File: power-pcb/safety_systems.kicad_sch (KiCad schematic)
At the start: 41 parts, among them J12 Conn_01x06, J13 Conn_01x03, J15 Conn_01x02, J17 Screw_Terminal_01x04, J18 Screw_Terminal_01x02, K1 G5Q-1A, K2 G5Q-1A, Q1 AO3400A, Q2 AO3400A, Q3 AO3400A, U22 NCV7357D13R2G, U23 74AHC1G08

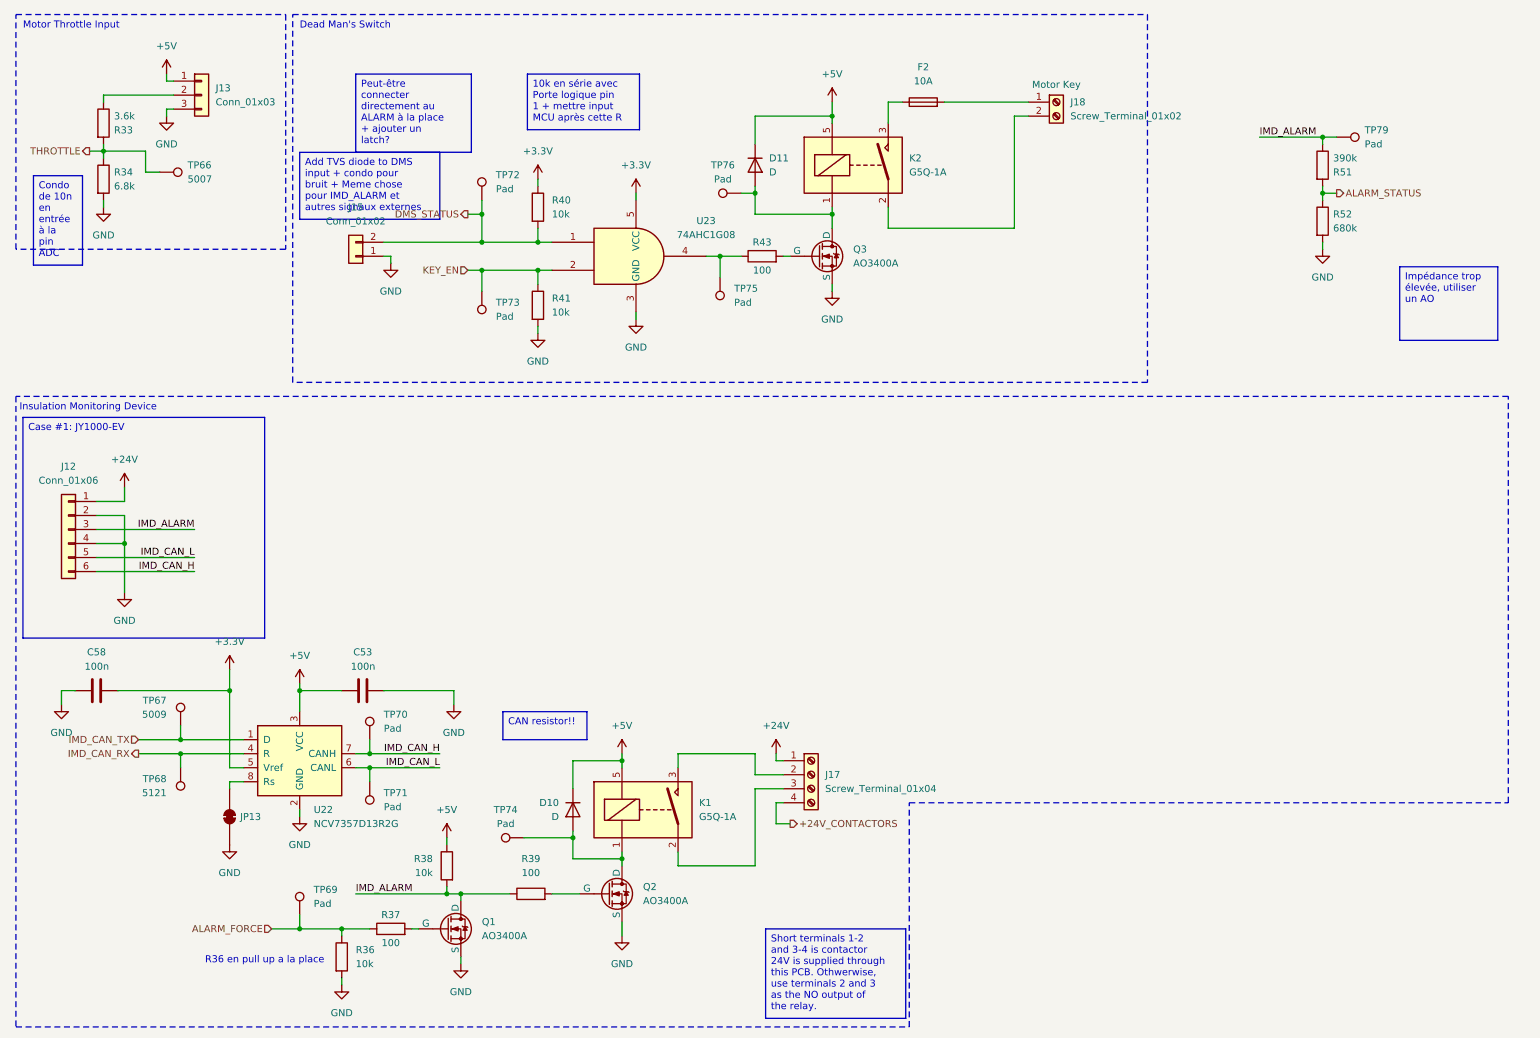
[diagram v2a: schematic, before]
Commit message: power-pcb: finish schematic layout
All parts are placed and connected, ERC passes (except for two
exclusions with comment).
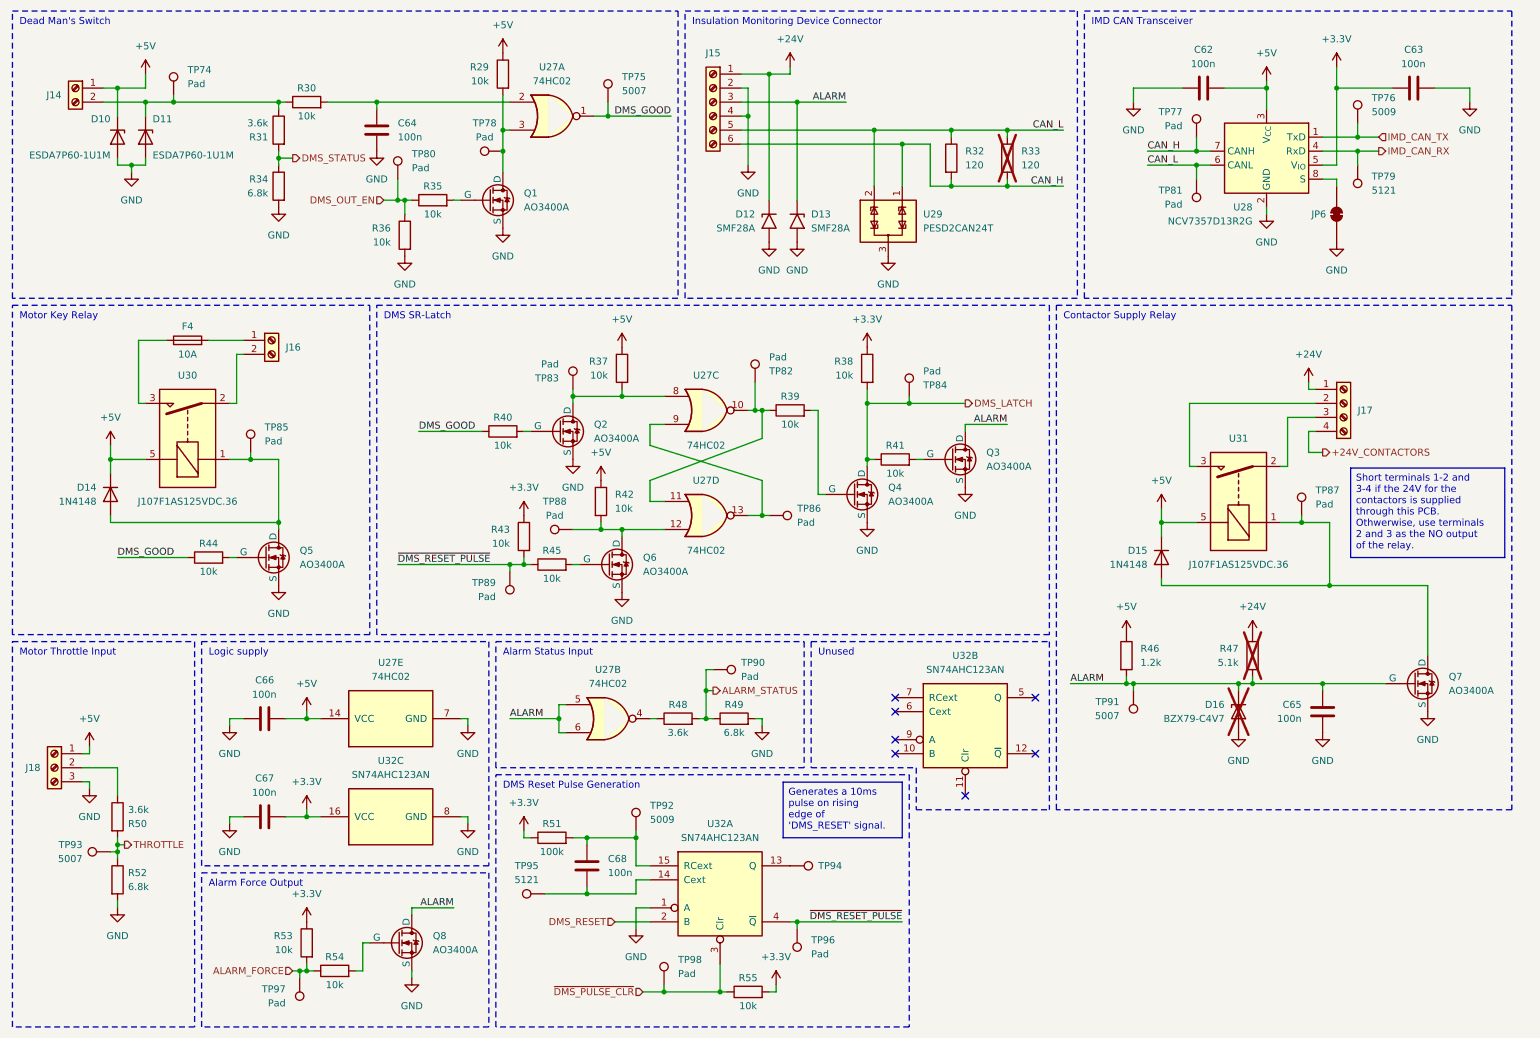
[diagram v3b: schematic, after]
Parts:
- removed C53, C58: 100n, Capacitor_SMD:C_0603_1608Metric_Pad1.08x0.95mm_HandSolder, symbol Device:C
- removed D10: D, symbol Device:D
- removed J12: Conn_01x06, symbol Connector_Generic:Conn_01x06
- removed J13: Conn_01x03, symbol Connector_Generic:Conn_01x03
- removed J15: Conn_01x02, symbol Connector_Generic:Conn_01x02
- removed JP13: SolderJumper_2_Bridged, symbol Jumper:SolderJumper_2_Bridged
- removed K1, K2: G5Q-1A, Relay_THT:Relay_SPST_Omron-G5Q-1A, symbol Relay:G5Q-1A
- removed R52: 680k, Resistor_SMD:R_0603_1608Metric, symbol Device:R
- removed TP67: 5009, symbol Connector:TestPoint
- removed TP68: 5121, symbol Connector:TestPoint
- removed TP70, TP71, TP72, TP73: Pad, symbol Connector:TestPoint
- removed U22: NCV7357D13R2G, Package_SO:SOIC-8_3.9x4.9mm_P1.27mm, symbol Interface_CAN_LIN:SN65HVD230
- removed U23: 74AHC1G08, symbol 74xGxx:74AHC1G08
- added C62, C63, C64, C65, C66, C67: 100n, Capacitor_SMD:C_0603_1608Metric_Pad1.08x0.95mm_HandSolder, symbol Device:C
- added C68: 100n, symbol Device:C
- added D10, D11: ESDA7P60-1U1M, symbol Device:D_Zener
- added D12, D13: SMF28A, Diode_SMD:D_SMF, symbol Diode:SMF28A
- added D15: 1N4148, Diode_THT:D_DO-35_SOD27_P7.62mm_Horizontal, symbol Device:D
- added D16: BZX79-C4V7, symbol Device:D_Zener
- added J14: Screw_Terminal_01x02, symbol Connector:Screw_Terminal_01x02
- added J15: Screw_Terminal_01x06, symbol Connector:Screw_Terminal_01x06
- added J18: Screw_Terminal_01x03, symbol Connector:Screw_Terminal_01x03
- added JP6: SolderJumper_2_Bridged, symbol Jumper:SolderJumper_2_Bridged
- added Q1, Q3, Q4, Q6, Q7: AO3400A, Package_TO_SOT_SMD:SOT-23, symbol Simulation_SPICE:NMOS
- added R29, R30, R35, R36, R42, R44, R45, R54, R55: 10k, symbol Device:R
- added R31, R48: 3.6k, Resistor_SMD:R_0603_1608Metric, symbol Device:R
- added R32, R33: 120, symbol Device:R
- added R34, R49: 6.8k, Resistor_SMD:R_0603_1608Metric, symbol Device:R
- added R46: 1.2k, Resistor_SMD:R_0402_1005Metric, symbol Device:R
- added R47: 5.1k, symbol Device:R
- added TP76, TP92: 5009, symbol Connector:TestPoint
- added TP77, TP78, TP80, TP81, TP82, TP83, TP84, TP86, TP87, TP88, TP89, TP90, TP96, TP98: Pad, symbol Connector:TestPoint
- added TP91: 5007, symbol Connector:TestPoint
- added TP94: TestPoint, TestPoint:TestPoint_THTPad_D2.0mm_Drill1.0mm, symbol Connector:TestPoint
- added TP95: 5121, symbol Connector:TestPoint
- added U27: 74HC02, symbol 74xx:74HC02
- added U28: NCV7357D13R2G, Package_SO:SOIC-8_3.9x4.9mm_P1.27mm, symbol Exocet:NCV7357
- added U29: PESD2CAN24T, Package_TO_SOT_SMD:SOT-23_Handsoldering, symbol Exocet:PESD2CAN
- added U30, U31: J107F1AS125VDC.36, Relay_THT:Relay_SPDT_Omron-G5LE-1, symbol Exocet:J107F1AS
- added U32: SN74AHC123AN, Package_DIP:DIP-16_W7.62mm_LongPads, symbol 74xx:74AHCT123
- D14: renamed from D11; value D -> 1N4148; footprint (none) -> Diode_THT:D_DO-35_SOD27_P7.62mm_Horizontal
- R37, R39, R43: value 100 -> 10k
- R51: value 390k -> 100k; footprint Resistor_SMD:R_0603_1608Metric -> (none)
- TP75: value Pad -> 5007
- TP79: value Pad -> 5121
- renumbered F2 to F4, J18 to J16, Q3 to Q5, Q1 to Q8, R33 to R50, R34 to R52, R36 to R53, TP76 to TP85, TP66 to TP93, TP69 to TP97
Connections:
- net +24V: now also D12.1 (A1), J15.1 (Pin_1), R47.1
- net +3.3V: now also R38.1, R43.1, R51.1, R53.1, C63.1, C67.2, R55.2, U28.5 (V_{IO}), U32.16 (VCC); no longer R40.1
- net +5V: now also R37.1, C62.2, C66.2, D10.1 (K), D15.1 (K), J14.1 (Pin_1), J18.1 (Pin_1), R29.1, R42.1, R46.1, U27.14 (VCC), U28.3 (V_{CC}), U30.5, U31.5; no longer R38.1
- net ALARM_FORCE: now also R53.2, R54.1; no longer R37.1, R53.1
- net ALARM_STATUS: now also R48.2, R49.1, TP90.1; no longer R51.2
- net DMS_STATUS: now also R31.2, R34.1; no longer R40.2
- net GND: now also C62.1, C63.2, C64.2, C65.2, C66.1, C67.1, D10.2 (A), D11.2 (A), D12.2 (A2), D13.2 (A2), D16.2 (A), J15.2 (Pin_2), J15.4 (Pin_4), J18.3 (Pin_3), JP6.1 (A), Q1.3 (S), Q3.3 (S), Q4.3 (S), Q6.3 (S), Q7.3 (S), R34.2, R36.2, R49.2, U27.7 (GND), U28.2 (GND), U29.3, U32.1 (A), U32.8 (GND); no longer R41.2, R53.2
- net IMD_CAN_RX: now also TP79.1, U28.4 (RxD)
- net IMD_CAN_TX: now also TP76.1, U28.1 (TxD)
- net at J17.2 (Pin_2): now also U31.3
- net at J17.3 (Pin_3): now also U31.2
- net at R37.2: now also Q2.1 (D), TP83.1, U27.8; no longer Q8.2 (G)
- net at D14.2 (A), Q5.1 (D), TP85.1: now also U30.1
- net at J16.2 (Pin_2): now also U30.2
- net at F4.1: now also U30.3
- net at TP74.1: now also D11.1 (K), J14.2 (Pin_2), R30.1, R31.1; no longer Q2.1 (D)
- net DMS_GOOD: now reaches TP75.1
- net DMS_GOOD: now also R40.1, R44.1, U27.1; no longer R43.1
- net at Q5.2 (G): now also R44.2; no longer R43.2
- net at Q2.2 (G): now also R40.2; no longer R39.2
- net at R50.1: now also J18.2 (Pin_2)
- removed net IMD_ALARM: Q8.1 (D), R38.2, R39.1, R51.1, TP79.1
- net KEY_EN renamed DMS_LATCH
- net DMS_LATCH: now also R38.2, Q4.1 (D), TP84.1
- new net: R48.1, U27.4
- new net: TP86.1, U27.13, U27.9
- new net: JP6.2 (B), U28.8 (S)
- new net: Q1.2 (G), R35.2
- new net: Q6.1 (D), R42.2, TP88.1, U27.12
- new net: C68.2, TP95.1, U32.14 (Cext)
- new net: D15.2 (A), Q7.1 (D), TP87.1, U31.1
- new net: R39.1, TP82.1, U27.10, U27.11
- new net: Q4.2 (G), R39.2
- new net: C68.1, R51.2, TP92.1, U32.15 (RCext)
- new net: Q8.2 (G), R54.2
- new net: Q6.2 (G), R45.2
- new net: TP94.1, U32.13 (Q)
- new net: Q3.2 (G), R41.2
- new net: Q1.1 (D), R29.2, TP78.1, U27.3
- new net: C64.1, R30.2, U27.2
- new net ALARM: C65.1, D13.1 (A1), D16.1 (K), J15.3 (Pin_3), Q3.1 (D), Q7.2 (G), Q8.1 (D), R46.2, R47.2, TP91.1, U27.5, U27.6
- new net CAN_H: J15.6 (Pin_6), R32.2, R33.2, TP77.1, U28.7 (CANH), U29.1
- new net CAN_L: J15.5 (Pin_5), R32.1, R33.1, TP81.1, U28.6 (CANL), U29.2
- new net DMS_OUT_EN: R35.1, R36.1, TP80.1
- new net DMS_RESET: U32.2 (B)
- new net ~{DMS_PULSE_CLR}: R55.1, TP98.1, U32.3 (Clr)
- new net ~{DMS_RESET_PULSE}: R43.2, R45.1, TP89.1, TP96.1, U32.4 (~{Q})
- no-connect marks 0 -> 7
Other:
- note added: "Alarm Force Output"
- note added: "Alarm Status Input"
- note added: "Contactor Supply Relay"
- note added: "DMS Reset Pulse Generation"
- note added: "DMS SR-Latch"
- note added: "IMD CAN Transceiver"
- note added: "Insulation Monitoring Device Connector"
- note added: "Logic supply"
- note added: "Motor Key Relay"
- note added: "Unused"
- note removed: "Insulation Monitoring Device"
- note removed: "R36 en pull up a la place"
- moved on the sheet: D14, F4, J16, J17, Q5, Q8, R50, R52, R53, TP85, TP93, TP97

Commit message: power-pcb: finish assigning JLCPCB PN
Also assigned missing footprints.
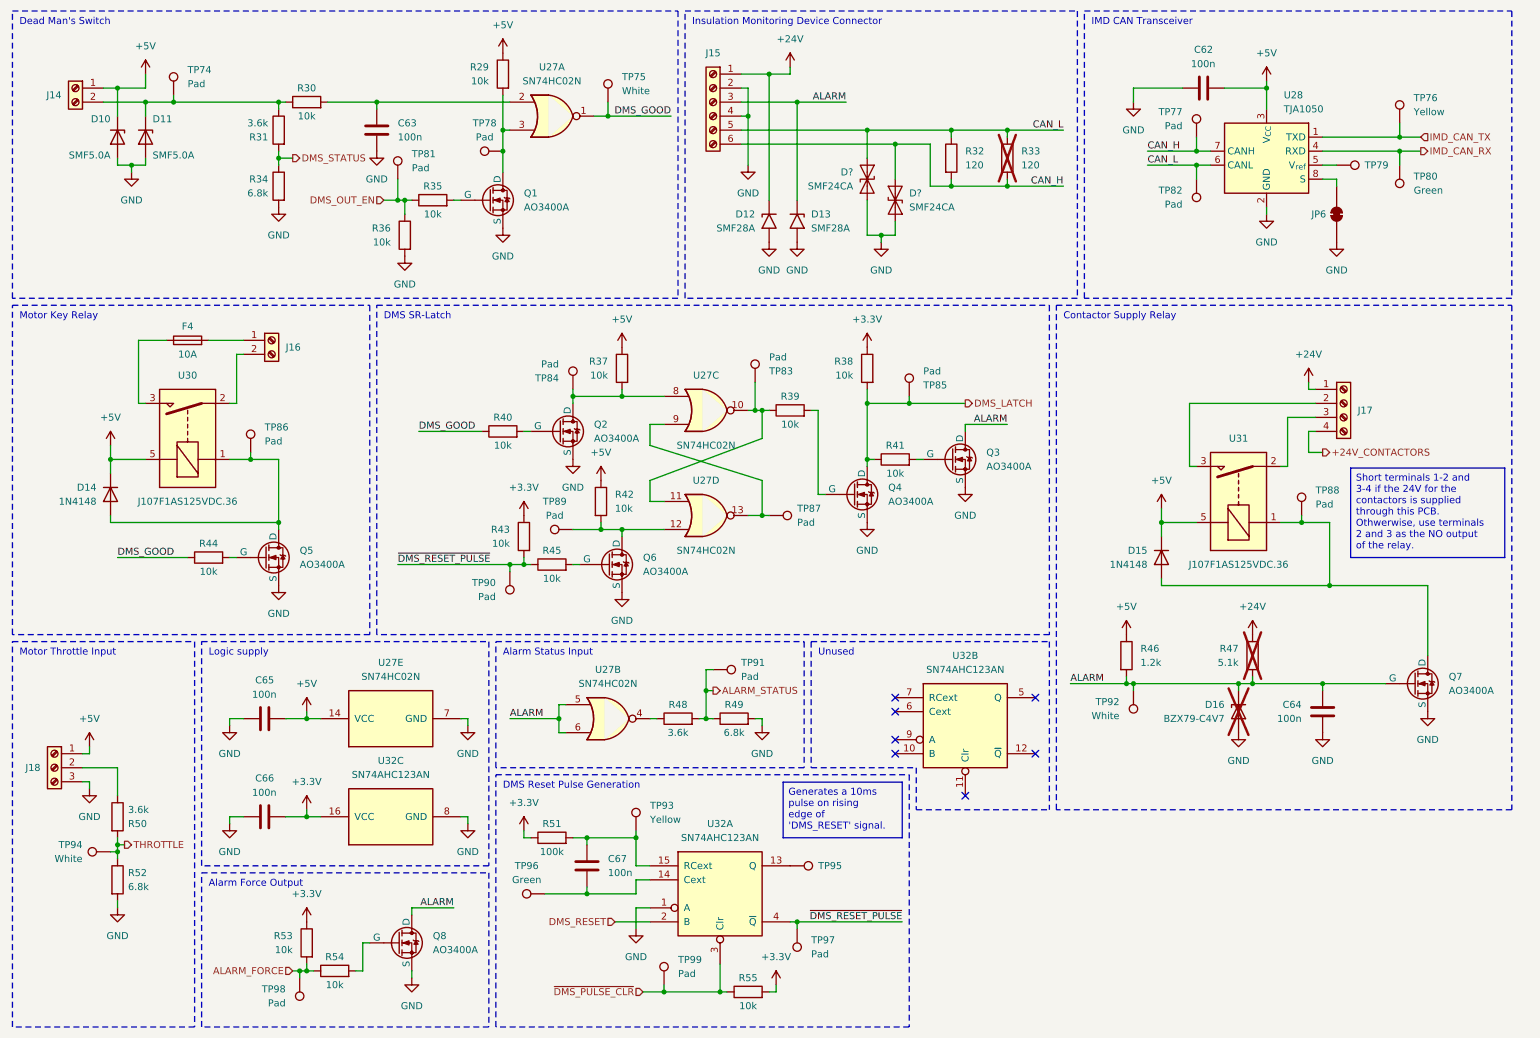
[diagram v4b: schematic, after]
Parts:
- removed C63: 100n, Capacitor_SMD:C_0603_1608Metric_Pad1.08x0.95mm_HandSolder, symbol Device:C
- removed U28: NCV7357D13R2G, Package_SO:SOIC-8_3.9x4.9mm_P1.27mm, symbol Exocet:NCV7357
- removed U29: PESD2CAN24T, Package_TO_SOT_SMD:SOT-23_Handsoldering, symbol Exocet:PESD2CAN
- added D? (x2): SMF24CA, Diode_SMD:D_SOD-123F, symbol Diode:SMAJ24CA
- added TP79: Hole, TestPoint:TestPoint_THTPad_D2.0mm_Drill1.0mm, symbol Connector:TestPoint
- added U28: TJA1050, Package_SO:SOIC-8_3.9x4.9mm_P1.27mm, symbol Exocet:TJA1050
- C67: renamed from C68; footprint (none) -> Capacitor_SMD:C_0603_1608Metric_Pad1.08x0.95mm_HandSolder; JLCPCB (none) -> C14663
- D10, D11: value ESDA7P60-1U1M -> SMF5.0A; footprint (none) -> Diode_SMD:D_SOD-123F; JLCPCB C1975146 -> C19077497
- D12, D13: JLCPCB (none) -> C41376091
- D14, D15: MFR (none) -> onsemi; MPN (none) -> 1N4148
- D16: footprint (none) -> Diode_THT:D_DO-35_SOD27_P7.62mm_Horizontal; MFR (none) -> Nexperia USA Inc.; MPN (none) -> BZX79-C4V7,133
- F4: footprint (none) -> Exocet:Fuseholder_Littelfuse_Combined; MFR (none) -> Littelfuse Inc.; MPN (none) -> 01110501Z
- J14, J16: footprint (none) -> Exocet:Wuerth_Term_Blk_2pos_Side_Entry_5mm; MFR (none) -> Wuerth Eletronik; MPN (none) -> 691137710002
- J15: footprint (none) -> Exocet:Wuerth_Term_Blk_6pos_Side_Entry_5mm; MFR (none) -> Wuerth Eletronik; MPN (none) -> 691137710006
- J17: footprint (none) -> Exocet:Wuerth_Term_Blk_4pos_Side_Entry_5mm; MFR (none) -> Wuerth Eletronik; MPN (none) -> 691137710004
- J18: footprint (none) -> Exocet:Wuerth_Term_Blk_3pos_Side_Entry_5mm; MFR (none) -> Wuerth Eletronik; MPN (none) -> 691137710003
- JP6: footprint (none) -> Jumper:SolderJumper-2_P1.3mm_Bridged_Pad1.0x1.5mm
- R29, R30, R35, R36, R37, R38, R39, R40, R41, R42, R43, R44, R45, R53, R54, R55: footprint (none) -> Resistor_SMD:R_0603_1608Metric_Pad0.98x0.95mm_HandSolder; JLCPCB (none) -> C25804
- R31, R34, R48, R49, R50, R52: footprint Resistor_SMD:R_0603_1608Metric -> Resistor_SMD:R_0603_1608Metric_Pad0.98x0.95mm_HandSolder
- R32, R33: footprint (none) -> Resistor_THT:R_Axial_DIN0309_L9.0mm_D3.2mm_P12.70mm_Horizontal; MFR (none) -> Stackpole Electronics Inc; MPN (none) -> CF12JT120R
- R46: footprint Resistor_SMD:R_0402_1005Metric -> Resistor_SMD:R_0603_1608Metric_Pad0.98x0.95mm_HandSolder; JLCPCB (none) -> C22765
- R47: footprint (none) -> Resistor_SMD:R_0402_1005Metric_Pad0.72x0.64mm_HandSolder; JLCPCB (none) -> C25905
- R51: footprint (none) -> Resistor_SMD:R_0603_1608Metric_Pad0.98x0.95mm_HandSolder; JLCPCB (none) -> C25803
- TP74, TP77, TP78: footprint (none) -> TestPoint:TestPoint_Pad_D1.5mm; now left out of the parts list
- TP75: value 5007 -> White; footprint (none) -> TestPoint:TestPoint_Keystone_5005-5009_Compact; MFR (none) -> Keystone Electronics; MPN (none) -> 5007
- TP76: value 5009 -> Yellow; footprint (none) -> TestPoint:TestPoint_Keystone_5005-5009_Compact; MFR (none) -> Keystone Electronics; MPN (none) -> 5009
- TP80: renamed from TP79; value 5121 -> Green; footprint (none) -> TestPoint:TestPoint_Keystone_5005-5009_Compact; MFR (none) -> Keystone Electronics; MPN (none) -> 5121
- TP81: renamed from TP80; footprint (none) -> TestPoint:TestPoint_Pad_D1.5mm; now left out of the parts list
- TP82: renamed from TP81; footprint (none) -> TestPoint:TestPoint_Pad_D1.5mm; now left out of the parts list
- TP83: renamed from TP82; footprint (none) -> TestPoint:TestPoint_Pad_D1.5mm; now left out of the parts list
- TP84: renamed from TP83; footprint (none) -> TestPoint:TestPoint_Pad_D1.5mm; now left out of the parts list
- TP85: renamed from TP84; footprint (none) -> TestPoint:TestPoint_Pad_D1.5mm; now left out of the parts list
- TP86: renamed from TP85; footprint (none) -> TestPoint:TestPoint_Pad_D1.5mm; now left out of the parts list
- TP87: renamed from TP86; footprint (none) -> TestPoint:TestPoint_Pad_D1.5mm; now left out of the parts list
- TP88: renamed from TP87; footprint (none) -> TestPoint:TestPoint_Pad_D1.5mm; now left out of the parts list
- TP89: renamed from TP88; footprint (none) -> TestPoint:TestPoint_Pad_D1.5mm; now left out of the parts list
- TP90: renamed from TP89; footprint (none) -> TestPoint:TestPoint_Pad_D1.5mm; now left out of the parts list
- TP91: renamed from TP90; footprint (none) -> TestPoint:TestPoint_Pad_D1.5mm; now left out of the parts list
- TP92: renamed from TP91; value 5007 -> White; footprint (none) -> TestPoint:TestPoint_Keystone_5005-5009_Compact; MFR (none) -> Keystone Electronics; MPN (none) -> 5007
- TP93: renamed from TP92; value 5009 -> Yellow; footprint (none) -> TestPoint:TestPoint_Keystone_5005-5009_Compact; MFR (none) -> Keystone Electronics; MPN (none) -> 5009
- TP94: renamed from TP93; value 5007 -> White; footprint (none) -> TestPoint:TestPoint_Keystone_5005-5009_Compact; MFR (none) -> Keystone Electronics; MPN (none) -> 5007
- TP95: renamed from TP94; value TestPoint -> Hole
- TP96: renamed from TP95; value 5121 -> Green; footprint (none) -> TestPoint:TestPoint_Keystone_5005-5009_Compact; MFR (none) -> Keystone Electronics; MPN (none) -> 5121
- TP97: renamed from TP96; footprint (none) -> TestPoint:TestPoint_Pad_D1.5mm; now left out of the parts list
- TP98: renamed from TP97; footprint (none) -> TestPoint:TestPoint_Pad_D1.5mm; now left out of the parts list
- TP99: renamed from TP98; footprint (none) -> TestPoint:TestPoint_Pad_D1.5mm; now left out of the parts list
- U27: value 74HC02 -> SN74HC02N; footprint (none) -> Package_DIP:DIP-14_W7.62mm_LongPads; MFR (none) -> Texas Instruments; MPN (none) -> SN74HC02N
- U30, U31: MFR (none) -> CIT Relay and Switch; MPN (none) -> J107F1AS125VDC.36
- U32: MFR (none) -> Texas Instruments; MPN (none) -> SN74AHC123AN
- renumbered C64 to C63, C65 to C64, C66 to C65, C67 to C66
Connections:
- net +5V: now also U28.3 (V_{CC})
- net CAN_H: now also D?.2 (A2), U28.7 (CANH)
- net CAN_L: now also D?.2 (A2), U28.6 (CANL)
- net GND: now also D?.1 (A1), D?.1 (A1), U28.2 (GND)
- net IMD_CAN_RX: now also U28.4 (RXD)
- net IMD_CAN_TX: now also U28.1 (TXD)
- net at JP6.2 (B): now also U28.8 (S)
- new net: TP79.1, U28.5 (V_{ref})
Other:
- moved on the sheet: TP76, TP80
